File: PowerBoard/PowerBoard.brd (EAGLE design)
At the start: 60 x 60 mm, 88 parts, among them IC1 MCP16311, IC2 MCP16311, IC3 DS2431P, U1 BQ24090, U2 MCP1726, U3 ATTINY85V, X2 MICROMATCH-4, X3 MICROMATCH-4

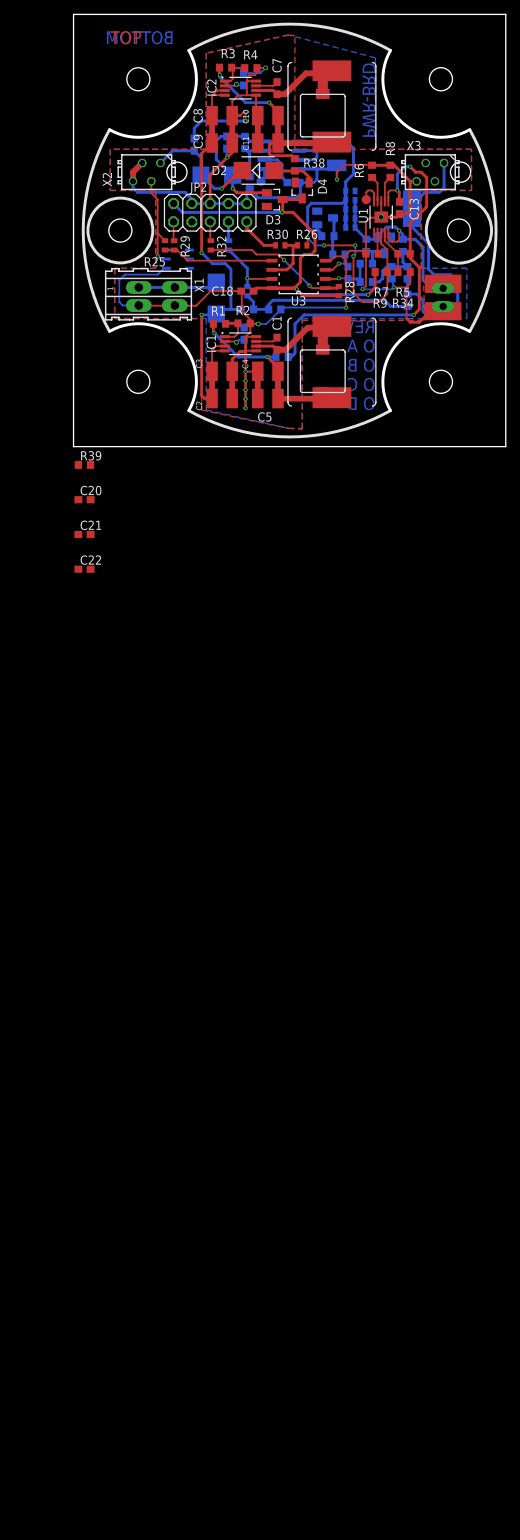
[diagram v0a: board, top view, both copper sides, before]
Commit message: Added inputs for Rev2 of PowerBoard to schematic
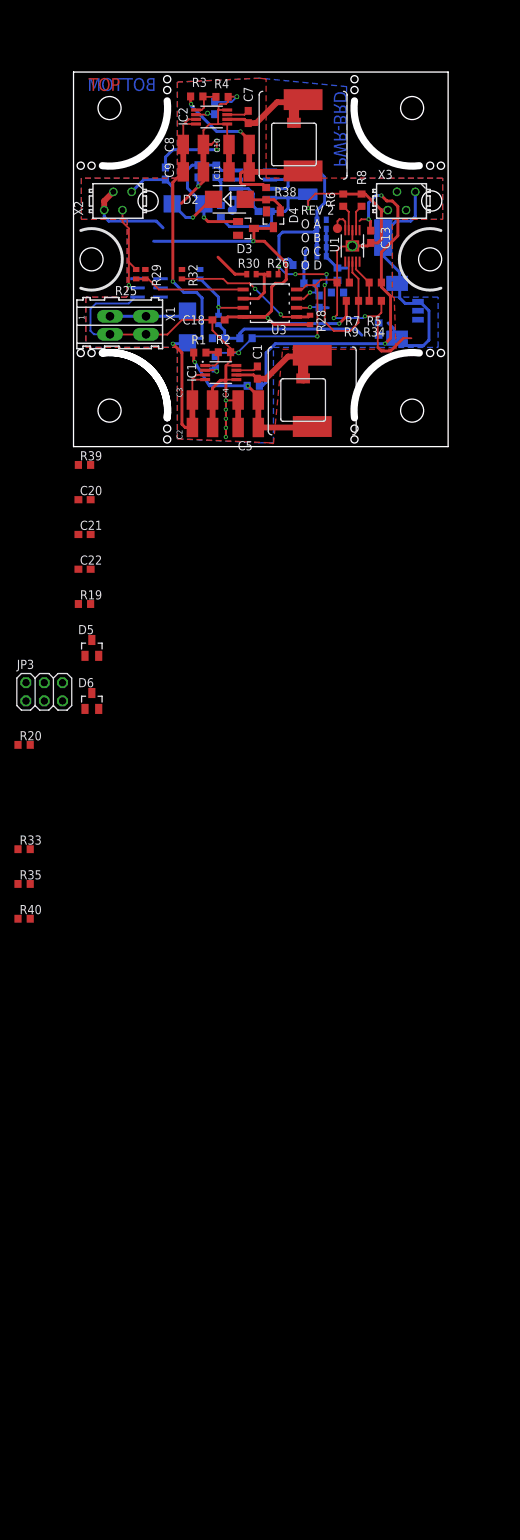
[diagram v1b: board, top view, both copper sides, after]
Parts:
- removed JP1: BATT, pinhead:1X02
- removed JP2: (no value), pinhead:2X05
- removed PAD2, PAD3: WIREPADSMD2,54-5,08, wirepad:SMD2,54-5,08
- added JP3: (no value), pinhead:2X03
- added P1: 0532610371, 0532610371:MOLEX_0532610371
- added R40: 0, rcl:R0603
- C10, C11, C4, C5: value 10u -> 22u
- D5, D6: value BAT54* -> BAT54
- L2: value L-EUPIS47XX_22u -> L-EUPIS47XX_22u*
- L4: value L-EUPIS47XX_15u -> L-EUPIS47XX_15u*
- R20: value 20k -> 0
- R21: value 0* -> 20k
- R25, R26, R27: value 0 -> 22
- R33: value 100 -> 0
- R36: value 0* -> 100k
- moved R35 100.1 mm to (-6.86, -60.7), flipped to the top, turned to 0 degrees
- moved R33 92.0 mm to (-6.86, -55.9), flipped to the top
- moved R20 83.1 mm to (-6.86, -41.4), flipped to the top, turned to 0 degrees
- moved D6 74.5 mm to (2.54, -35.3), flipped to the top, turned to 0 degrees
- moved D5 69.1 mm to (2.54, -27.9), flipped to the top, turned to 0 degrees
- moved R19 66.6 mm to (1.52, -21.8), flipped to the top, turned to 0 degrees
- moved C13 5.66 mm to (41.2, 29.1)
- moved D4 5.66 mm to (27.8, 31.6)
- moved PAD1 5.66 mm to (43.0, 29.0)
- moved R13 5.66 mm to (34.4, 28.9)
- moved R16 5.66 mm to (34.4, 31.5)
- moved C10 5.66 mm to (23.0, 42.0)
- moved C11 5.66 mm to (23.0, 38.1)
- moved C12 5.66 mm to (19.6, 47.0)
- moved C14 5.66 mm to (32.5, 36.4)
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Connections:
- removed net BATT: D5.1, JP1.1, PAD2.1, R12.2, R13.2, R14.2, R15.2, R16.2, R19.2, R21.2, U1.10
- removed net LDO: C14.1, D6.1, R12.1, R13.1, R14.1, R15.1, R16.1, R23.2, U2.1, U2.2, U2.3
- removed net U_BA: C20.2, R19.1, R20.2, R33.1, R35.1
- new net BATT_CON: P1.1, R12.2, R13.2, R14.2, R15.2, R16.2, R21.2
- new net LDO_IN: C14.1, R12.1, R13.1, R14.1, R15.1, R16.1, R23.2, R33.1, U2.1, U2.2, U2.3
- new net N$27: C20.2, R19.2, R21.1, R22.2
- new net N$28: D5.3, R17.2
- new net N$29: R20.2, U1.1
- new net N$30: R33.2, R35.2, U1.10
- new net N$31: P1.3, R40.1
- net +12V: now also D5.1; no longer R17.2
- net +5V: now also R20.1; no longer U1.1
- net AVR_MISO: no longer JP2.9
- net AVR_MOSI: no longer JP2.1
- net AVR_RST: no longer JP2.5
- net AVR_SCK: no longer JP2.7
- net GND: now also JP3.6, P1.2, R19.1; no longer JP1.2, JP2.10, JP2.4, JP2.6, JP2.8, PAD3.1, R20.1
- net I_POS: no longer R33.2
- net N$13: now also R40.2
- net N$17: now also D6.3, R36.2; no longer D5.3, R21.1, R22.2
- net N$21: no longer D6.3
- net N$24: now also D6.1; no longer R35.2, R36.2
- net VCCINT: now also JP3.2; no longer JP2.2
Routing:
- net LDO: track 45.2 -> 0.00 mm
- net LDO_IN: track 0.00 -> 44.5 mm
- net BATT: track 28.6 -> 0.00 mm, vias 1 -> 0
- net GND: track 248.8 -> 233.0 mm
- net U_BA: track 9.03 -> 0.00 mm
- net BATT_CON: track 0.00 -> 7.41 mm
- net N$17: track 4.37 -> 0.00 mm
- net N$24: track 39.2 -> 35.8 mm
- net I_POS: track 7.62 -> 4.49 mm
- net AVR_SCK: track 2.64 -> 0.11 mm
- net AVR_RST: track 2.64 -> 0.11 mm
- net AVR_MOSI: track 2.64 -> 0.11 mm
- net U_12: track 24.9 -> 22.6 mm
- net VCCINT: track 64.6 -> 62.9 mm
- net +5V: track 54.8 -> 53.5 mm
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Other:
- board size 60 x 60 mm -> 52 x 52 mm
- board text added: "GLUE BATT"
- board text added: "REV 2 O A O B O C O D"
- board text removed: "REV 1 O A O B O C O D"

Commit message: Optical cleanup of the schematic, added ideal diodes and some other stuff from the TODO list
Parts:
- added IC4: DS28E05, 1wire:SOT23
- added Q1, Q3, Q4, Q6: BC857BSMD, transistor-pnp:SOT23-BEC
- added Q2, Q5: IRLML6402, IRLML6402:SOT23
- added R41, R43, R44, R46: 47k, rcl:R0603
- added R42, R45: 470k, rcl:R0603
- D1, D2: value SS24 -> SS24*
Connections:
- new net N$33: Q1.C, Q2.1, R43.2
- new net N$34: Q1.B, Q3.B, R42.2
- new net N$35: Q3.C, R41.2
- new net N$37: Q4.C, Q5.1, R44.2
- new net N$38: Q4.B, Q6.B, R45.2
- new net N$39: Q6.C, R46.2
- net +3V3: now also Q5.2, Q6.E
- net AVR_MISO: now also JP3.1
- net AVR_MOSI: now also JP3.4
- net AVR_RST: now also JP3.5
- net AVR_SCK: now also JP3.3
- net BATT_CON: now also R35.1
- net GND: now also IC4.3, R41.1, R42.1, R43.1, R44.1, R45.1, R46.1
- net ONEWIRE: now also IC4.1
- net V+: now also Q2.2, Q3.E
- net VCC: now also Q1.E, Q2.3, Q4.E, Q5.3
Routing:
- net VCC: track 16.7 -> 6.72 mm, vias 1 -> 0
- net +3V3: track 6.51 -> 5.88 mm
